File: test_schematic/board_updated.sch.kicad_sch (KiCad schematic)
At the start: 14 parts, among them SW1 SW_Push, SW2 SW_Push, SW3 SW_Push, SW4 SW_Push, SW5 SW_SPDT, SW6 SW_SPDT, U1 MCP4251-103E/P, U2 ESP32-S3-DEVKITC-1-N8R2, U3 MCP4251-103E/P, U4 MAX98357A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

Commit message: Bascially complete
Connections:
- net at SW1.1: now also U2.J3_13 (GPIO35)
- net at U2.J3_10 (GPIO38): now also SW4.1
- net at U2.J3_11 (GPIO37): now also SW3.1
- net at U2.J3_12 (GPIO36): now also SW2.1
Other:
- moved on the sheet: SW1, SW2, SW3, SW4, U5

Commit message: Added more labels
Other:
- note added: "ESP32"
- note added: "IMU"
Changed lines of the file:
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@@
+		)
+	)
+	(text "ESP32"
+		(exclude_from_sim no)
+		(at 122.936 67.056 0)
+		(effects
+			(font
+				(face "KiCad Font")
+				(size 1.27 1.27)
+				(thickness 0.254)
+				(bold yes)
+			)
 		)
 	)
@@
 		)
 	)
+	(text "IMU"
+		(exclude_from_sim no)
+		(at 241.046 108.458 0)
+		(effects
+			(font
+				(size 1.905 1.905)
+				(thickness 0.254)
+				(bold yes)
+			)
+		)
+	)
 	(text "Digipot (Left Joystick)"
 		(exclude_from_sim no)
@@
 			(font
 				(size 1.27 1.27)
+				(thickness 0.254)
+				(bold yes)
 			)
 		)
@@
 			(font
 				(size 1.27 1.27)
+				(thickness 0.254)
+				(bold yes)
 			)
 		)

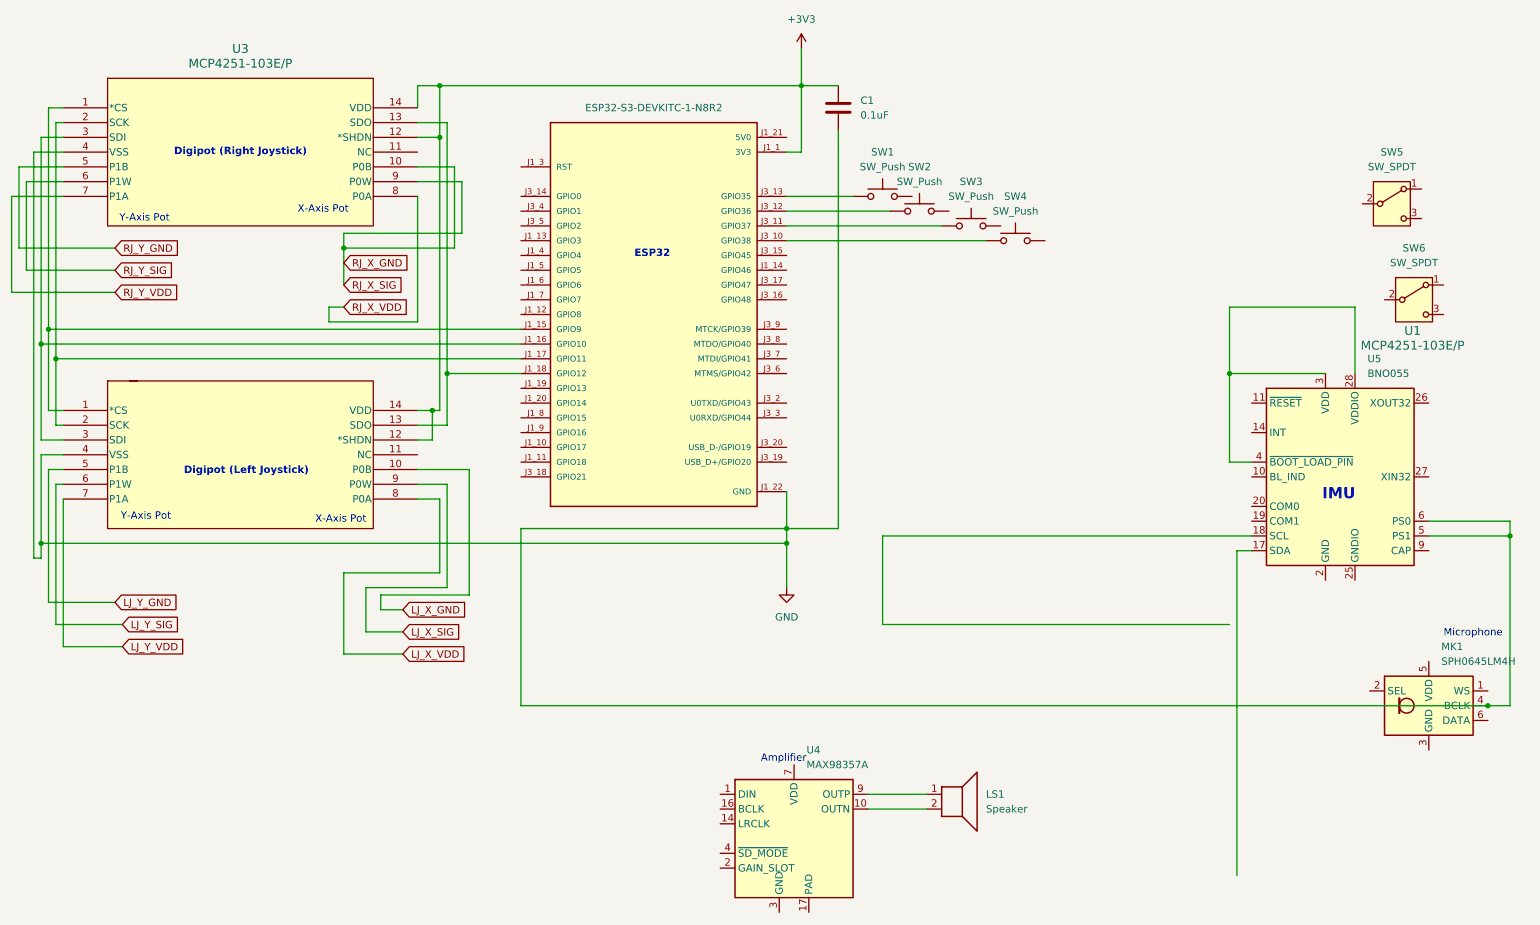
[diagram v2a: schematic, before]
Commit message: Update test schematic w/ imu
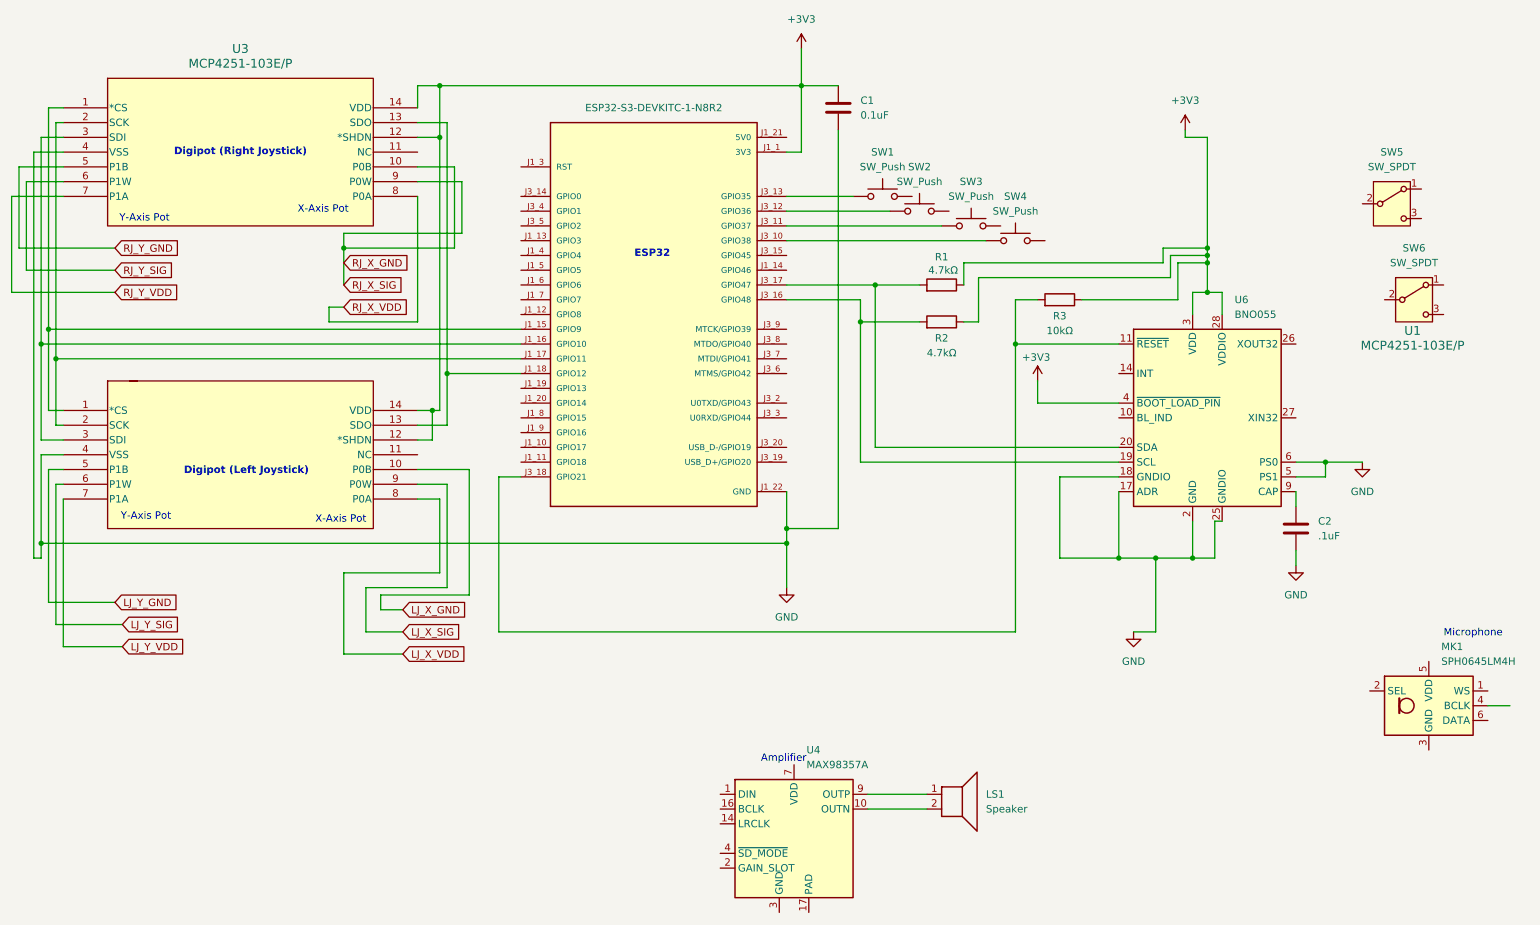
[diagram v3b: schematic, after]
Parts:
- removed U5: BNO055, Package_LGA:LGA-28_5.2x3.8mm_P0.5mm, symbol Sensor_Motion:BNO055
- added C2: .1uF, symbol Device:C
- added R1, R2: 4.7kΩ, symbol Device:R
- added R3: 10kΩ, symbol Device:R
- added U6: BNO055, Package_LGA:LGA-28_5.2x3.8mm_P0.5mm, symbol Sensor_Motion:BNO055
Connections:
- net +3V3: now also R1.2, R2.2, R3.2, U6.28 (VDDIO), U6.3 (VDD), U6.4 (~{BOOT_LOAD_PIN})
- net GND: now also C2.1, U6.17 (ADR), U6.18 (GNDIO), U6.2 (GND), U6.25 (GNDIO), U6.5 (PS1), U6.6 (PS0); no longer MK1.4 (BCLK)
- net at U2.J3_16 (GPIO48): now also R2.1, U6.19 (SCL)
- net at U2.J3_17 (GPIO47): now also R1.1, U6.20 (SDA)
- net at U2.J3_18 (GPIO21): now also R3.1, U6.11 (~{RESET})
- new net: C2.2, U6.9 (CAP)
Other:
- note removed: "IMU"
